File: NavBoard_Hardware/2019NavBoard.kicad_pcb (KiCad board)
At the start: 2 copper layers, 61 x 88.7 mm, 21 parts, among them J1 Conn_Coaxial, U2 12mm_Coin_Battery_Cell_Holder, U5 FGPMMOPA6H

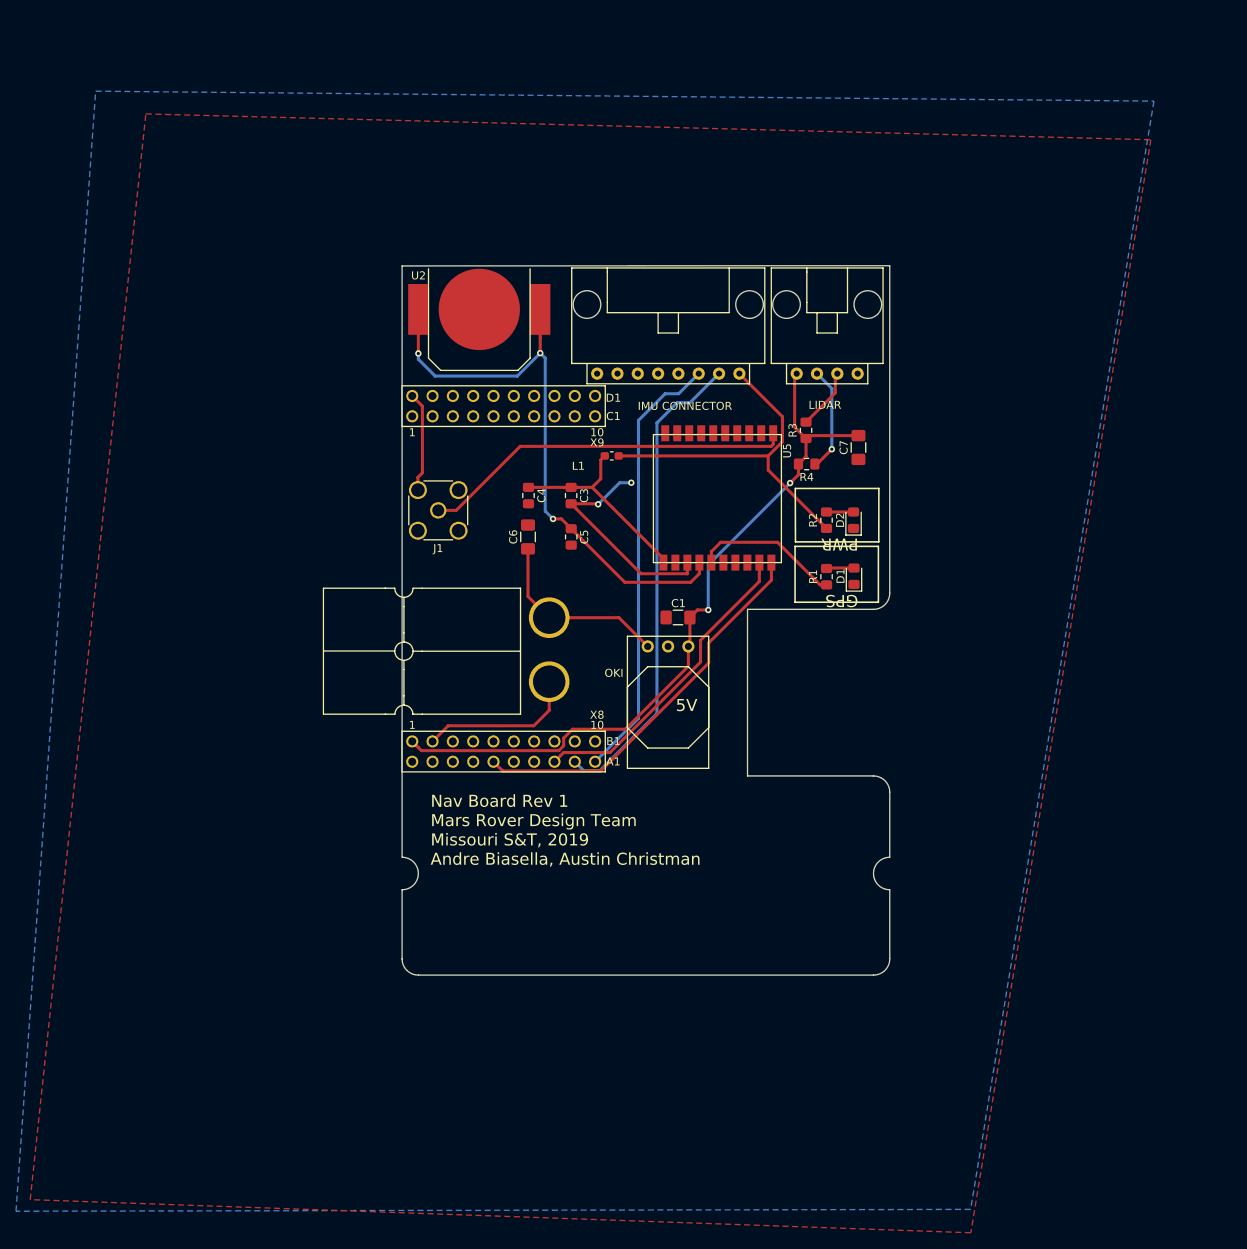
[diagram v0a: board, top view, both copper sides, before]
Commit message: Editied schematic and made PCB
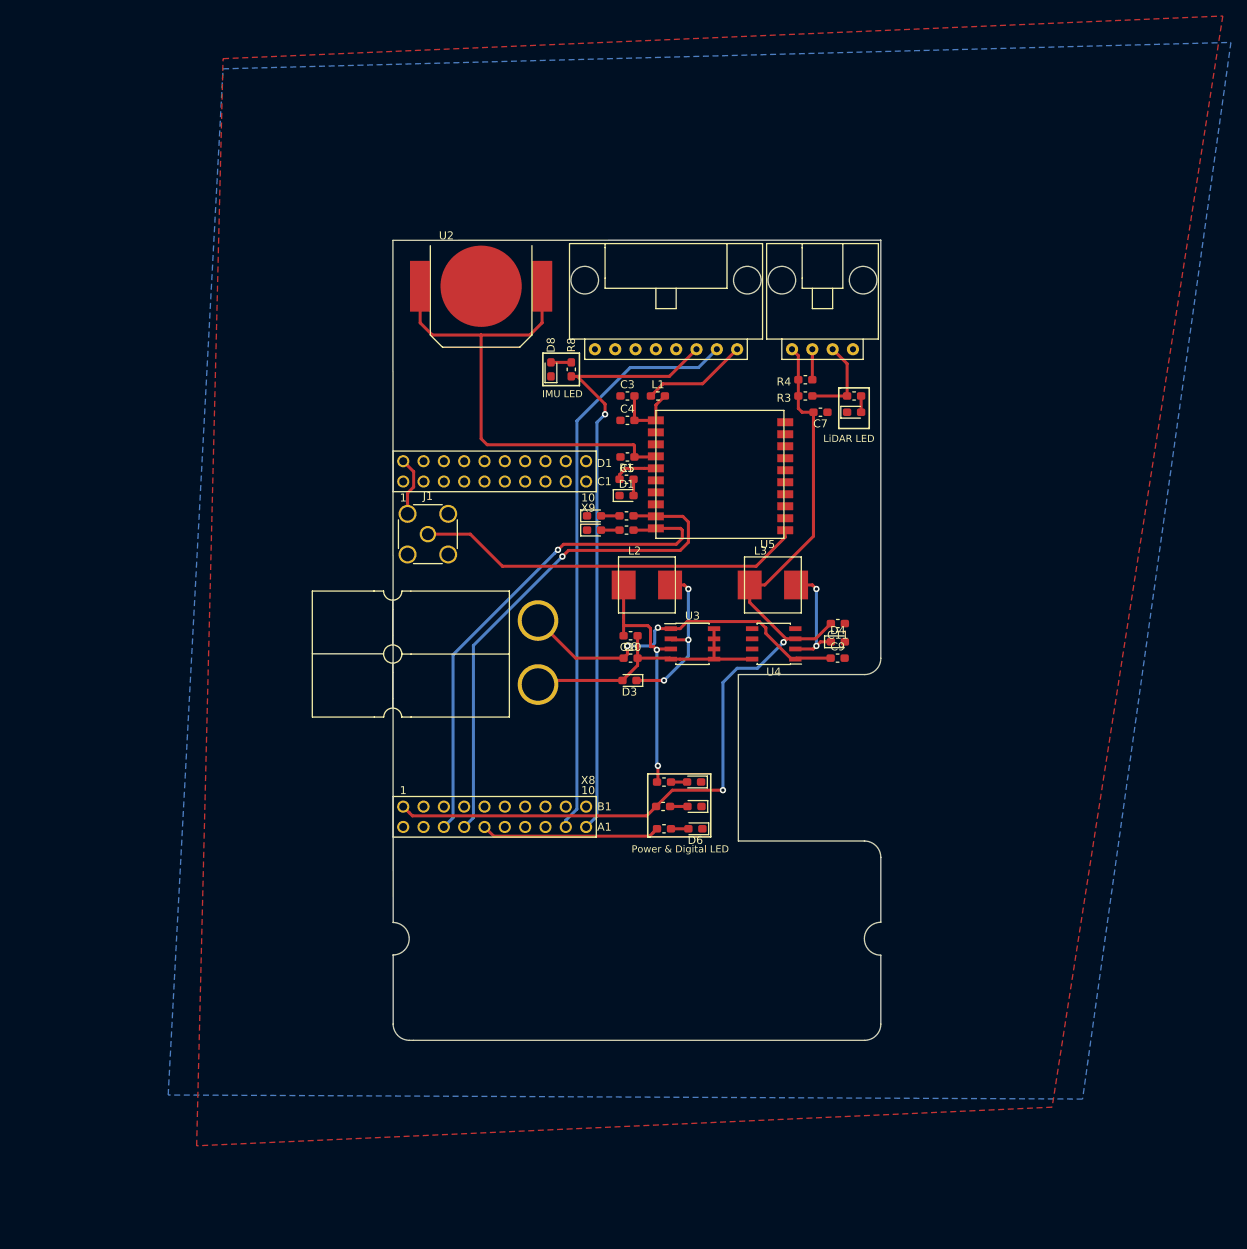
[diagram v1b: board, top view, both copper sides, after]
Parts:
- removed C1, C6: 10uF, Capacitor_SMD:C_1206_3216Metric_Pad1.42x1.75mm_HandSolder
- removed C2: OKI, MRDT_Devices:OKI_Horizontal
- removed IMU CONNECTOR: Molex_SL_08, MRDT_Connectors:MOLEX_SL_08_Horizontal
- removed LIDAR: LiDAR, MRDT_Connectors:MOLEX_SL_04_Horizontal
- added C10: 10u, Capacitor_SMD:C_0603_1608Metric_Pad1.05x0.95mm_HandSolder, F.Cu at (144.9, 101.9)
- added C11: 10u, Capacitor_SMD:C_0603_1608Metric_Pad1.05x0.95mm_HandSolder, F.Cu at (170.8, 100.3)
- added C8: 10u, Capacitor_SMD:C_0603_1608Metric_Pad1.05x0.95mm_HandSolder, F.Cu at (144.9, 104.6)
- added C9: 10u, Capacitor_SMD:C_0603_1608Metric_Pad1.05x0.95mm_HandSolder, F.Cu at (170.8, 104.6)
- added Conn2: LiDAR, MRDT_Connectors:MOLEX_SL_04_Horizontal, F.Cu at (168.9, 66.0)
- added Conn3: Molex_SL_08, MRDT_Connectors:MOLEX_SL_08_Horizontal, F.Cu at (149.4, 66.0)
- added D10: PWR, LED_SMD:LED_0603_1608Metric_Pad1.05x0.95mm_HandSolder, F.Cu at (140.3, 86.9)
- added D3: D_Schottky, Diode_SMD:D_0603_1608Metric_Pad1.05x0.95mm_HandSolder, F.Cu at (144.8, 107.4)
- added D4: D_Schottky, Diode_SMD:D_0603_1608Metric_Pad1.05x0.95mm_HandSolder, F.Cu at (170.8, 102.6)
- added D5: PWR, LED_SMD:LED_0603_1608Metric_Pad1.05x0.95mm_HandSolder, F.Cu at (152.9, 123.2)
- added D6: PWR, LED_SMD:LED_0603_1608Metric_Pad1.05x0.95mm_HandSolder, F.Cu at (153.0, 126.0)
- added D7: PWR, LED_SMD:LED_0603_1608Metric_Pad1.05x0.95mm_HandSolder, F.Cu at (172.9, 73.9)
- added D8: PWR, LED_SMD:LED_0603_1608Metric_Pad1.05x0.95mm_HandSolder, F.Cu at (135.0, 68.6)
- added D9: PWR, LED_SMD:LED_0603_1608Metric_Pad1.05x0.95mm_HandSolder, F.Cu at (140.3, 88.6)
- added L2: 47u, MRDT_Passives:ETQ-P4M470YFN_Inductor, F.Cu at (147.0, 95.5)
- added L3: 47u, MRDT_Passives:ETQ-P4M470YFN_Inductor, F.Cu at (162.7, 95.5)
- added R10: 500, Resistor_SMD:R_0603_1608Metric_Pad1.05x0.95mm_HandSolder, F.Cu at (144.4, 86.9)
- added R5: 500, Resistor_SMD:R_0603_1608Metric_Pad1.05x0.95mm_HandSolder, F.Cu at (149.0, 123.2)
- added R6: 500, Resistor_SMD:R_0603_1608Metric_Pad1.05x0.95mm_HandSolder, F.Cu at (149.1, 126.0)
- added R7: 500, Resistor_SMD:R_0603_1608Metric_Pad1.05x0.95mm_HandSolder, F.Cu at (172.9, 71.9)
- added R8: 500, Resistor_SMD:R_0603_1608Metric_Pad1.05x0.95mm_HandSolder, F.Cu at (137.5, 68.6)
- added R9: 500, Resistor_SMD:R_0603_1608Metric_Pad1.05x0.95mm_HandSolder, F.Cu at (144.4, 88.6)
- added U3: AP1059, Package_SO:SOIC-8_3.9x4.9mm_P1.27mm, F.Cu at (152.7, 102.9)
- added U4: AP1059, Package_SO:SOIC-8_3.9x4.9mm_P1.27mm, F.Cu at (162.8, 102.9)
- C3, C4, C5: footprint Capacitor_SMD:C_0805_2012Metric_Pad1.15x1.40mm_HandSolder -> Capacitor_SMD:C_0603_1608Metric_Pad1.05x0.95mm_HandSolder
- C7: footprint Capacitor_SMD:C_1206_3216Metric_Pad1.42x1.75mm_HandSolder -> Capacitor_SMD:C_0603_1608Metric_Pad1.05x0.95mm_HandSolder
- D1, D2: footprint LED_SMD:LED_0805_2012Metric_Pad1.15x1.40mm_HandSolder -> LED_SMD:LED_0603_1608Metric_Pad1.05x0.95mm_HandSolder
- R1, R3, R4: footprint Resistor_SMD:R_0805_2012Metric_Pad1.15x1.40mm_HandSolder -> Resistor_SMD:R_0603_1608Metric_Pad1.05x0.95mm_HandSolder
- R2: value 1K -> 500; footprint Resistor_SMD:R_0805_2012Metric_Pad1.15x1.40mm_HandSolder -> Resistor_SMD:R_0603_1608Metric_Pad1.05x0.95mm_HandSolder
- moved R2 38.5 mm to (149.1, 120.1), turned to 0 degrees
- moved D2 38.3 mm to (152.9, 120.1), turned to 180 degrees
- moved D1 30.2 mm to (144.4, 84.3), turned to 0 degrees
- moved R1 27.8 mm to (144.4, 82.3), turned to 0 degrees
- moved U5 17.8 mm to (148.1, 74.9), turned to 0 degrees
- moved C4 15.5 mm to (144.5, 74.9), turned to 0 degrees
- moved C3 14.3 mm to (144.5, 71.9), turned to 0 degrees
- moved C5 12.2 mm to (144.5, 79.5), turned to 180 degrees
- moved R4 10.5 mm to (166.8, 69.8)
- moved L1 9.45 mm to (148.3, 71.9), turned to 0 degrees
- moved U1 8.23 mm to (115.2, 127.0)
- moved C7 6.48 mm to (168.7, 73.9), turned to 180 degrees
- moved R3 4.29 mm to (166.8, 71.9), turned to 0 degrees
- moved J1 3.24 mm to (119.6, 89.2), turned to 0 degrees
- moved U2 2.90 mm to (126.2, 58.2)
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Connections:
- net 1PPS renamed Net-(U5-Pad13)
- net Net-(J1-Pad1) renamed /EXAnt
- C3 pad 1: Net-(C3-Pad1) -> GND
- C3 pad 2: GND -> Net-(C3-Pad2)
- C4 pad 1: Net-(C3-Pad1) -> GND
- C4 pad 2: GND -> Net-(C3-Pad2)
- Conn1 pad 1: GND -> Net-(C10-Pad1)
- L1 pad 2: Net-(C3-Pad1) -> Net-(C3-Pad2)
- U1 pad PC4: Net-(U1-PadPC4) -> TivaRX(7)
- U1 pad PC5: Net-(U1-PadPC5) -> TivaTX(7)
- U1 pad PC6: RX(7) -> Error_LED
- U1 pad PC7: TX(7) -> Net-(U1-PadPC7)
- U5 pad 1: Net-(C3-Pad1) -> Net-(C3-Pad2)
- U5 pad 10: RX(7) -> TivaRX(7)
- U5 pad 9: TX(7) -> TivaTX(7)
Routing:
- net TivaTX(7): track 0.00 -> 65.1 mm, vias 0 -> 1
- net TivaRX(7): track 0.00 -> 64.0 mm, vias 0 -> 1
- net GND: track 62.2 -> 7.44 mm, vias 2 -> 0
- net RX(7): track 48.8 -> 0.00 mm
- net TX(7): track 38.9 -> 0.00 mm
- net Net-(C10-Pad1): track 0.00 -> 35.3 mm
- net +5V: track 90.3 -> 116.3 mm
- net Net-(C3-Pad1): track 25.7 -> 0.00 mm
- net Error_LED: track 0.00 -> 22.4 mm
- net SDA(0): track 54.9 -> 75.8 mm, vias 0 -> 1
- net Net-(C8-Pad1): track 23.5 -> 44.4 mm, vias 0 -> 2
- net Net-(D3-Pad1): track 0.00 -> 20.9 mm, vias 0 -> 3
- net Net-(D4-Pad1): track 0.00 -> 14.7 mm, vias 0 -> 2
- net Net-(R1-Pad1): track 18.5 -> 5.45 mm
- net VBACKUP: track 74.2 -> 62.2 mm, vias 3 -> 0
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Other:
- board size 61 x 88.7 mm -> 61 x 100 mm
- board text added: "IMU LED"
- board text added: "LiDAR LED"
- board text added: "Power & Digital LED"
- board text removed: "5V"
- board text removed: "GPS"
- board text removed: "Nav Board Rev 1 Mars Rover Design Team Missouri S&T, 2019 Andre Biasella, Austin Christman"
- board text removed: "PWR"

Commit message: edit PCB
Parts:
- added G***: LOGO, MRDT_Silkscreens:MRDT_Logo_10mm, F.Cu at (120.9, 72.4)

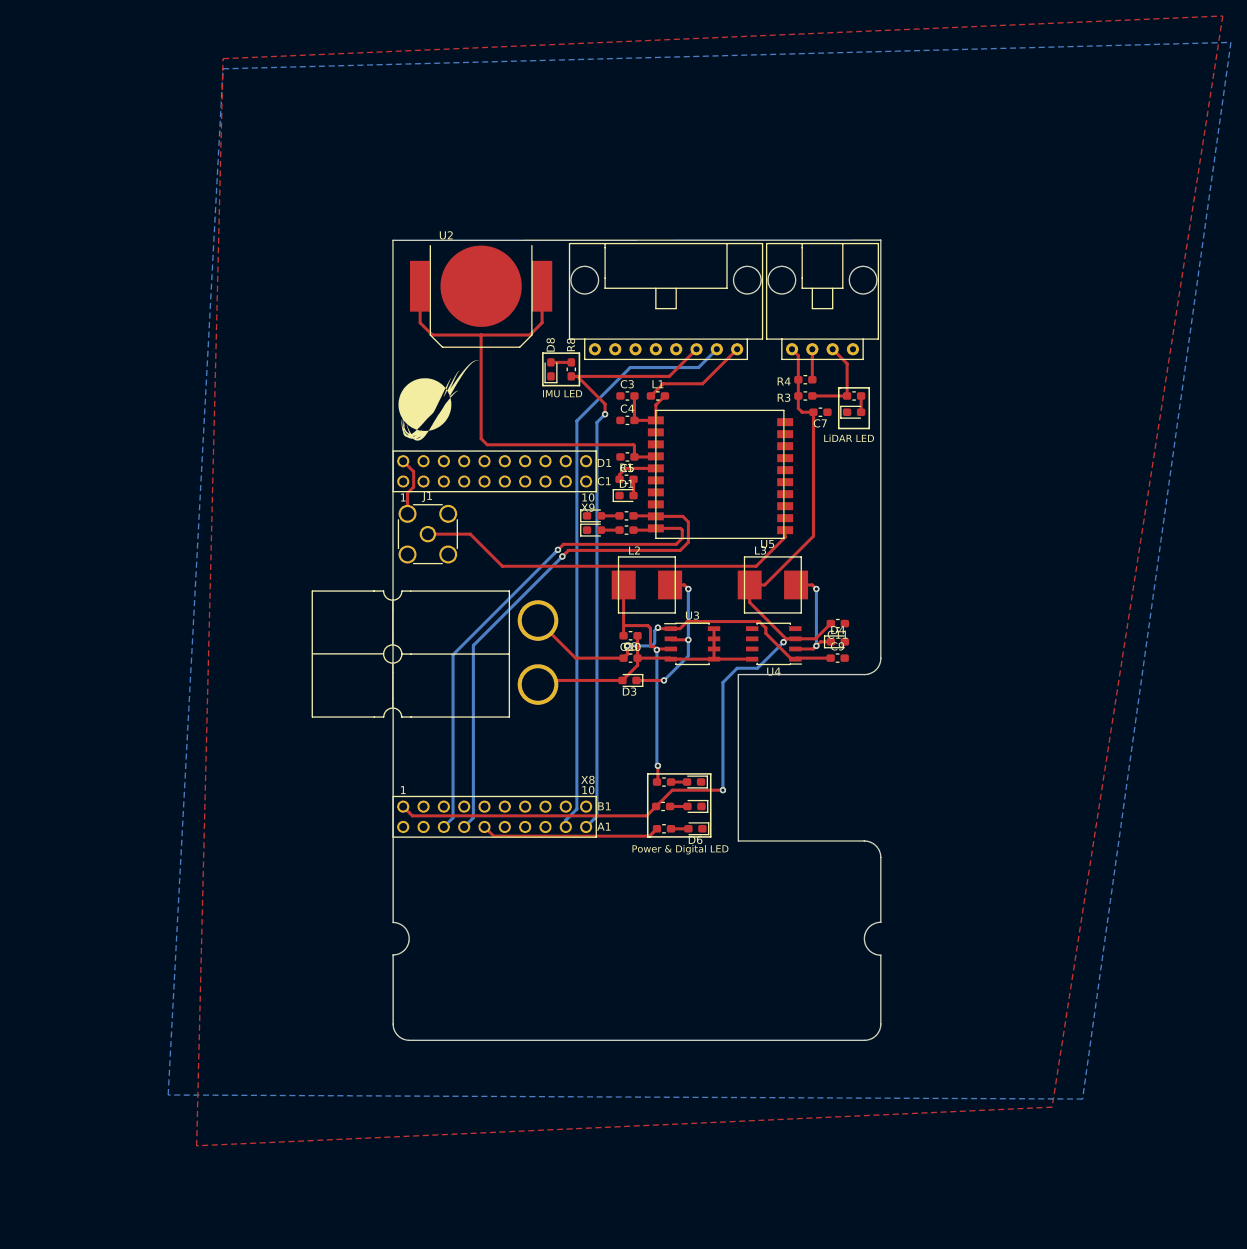
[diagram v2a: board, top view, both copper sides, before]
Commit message: Fixed traces
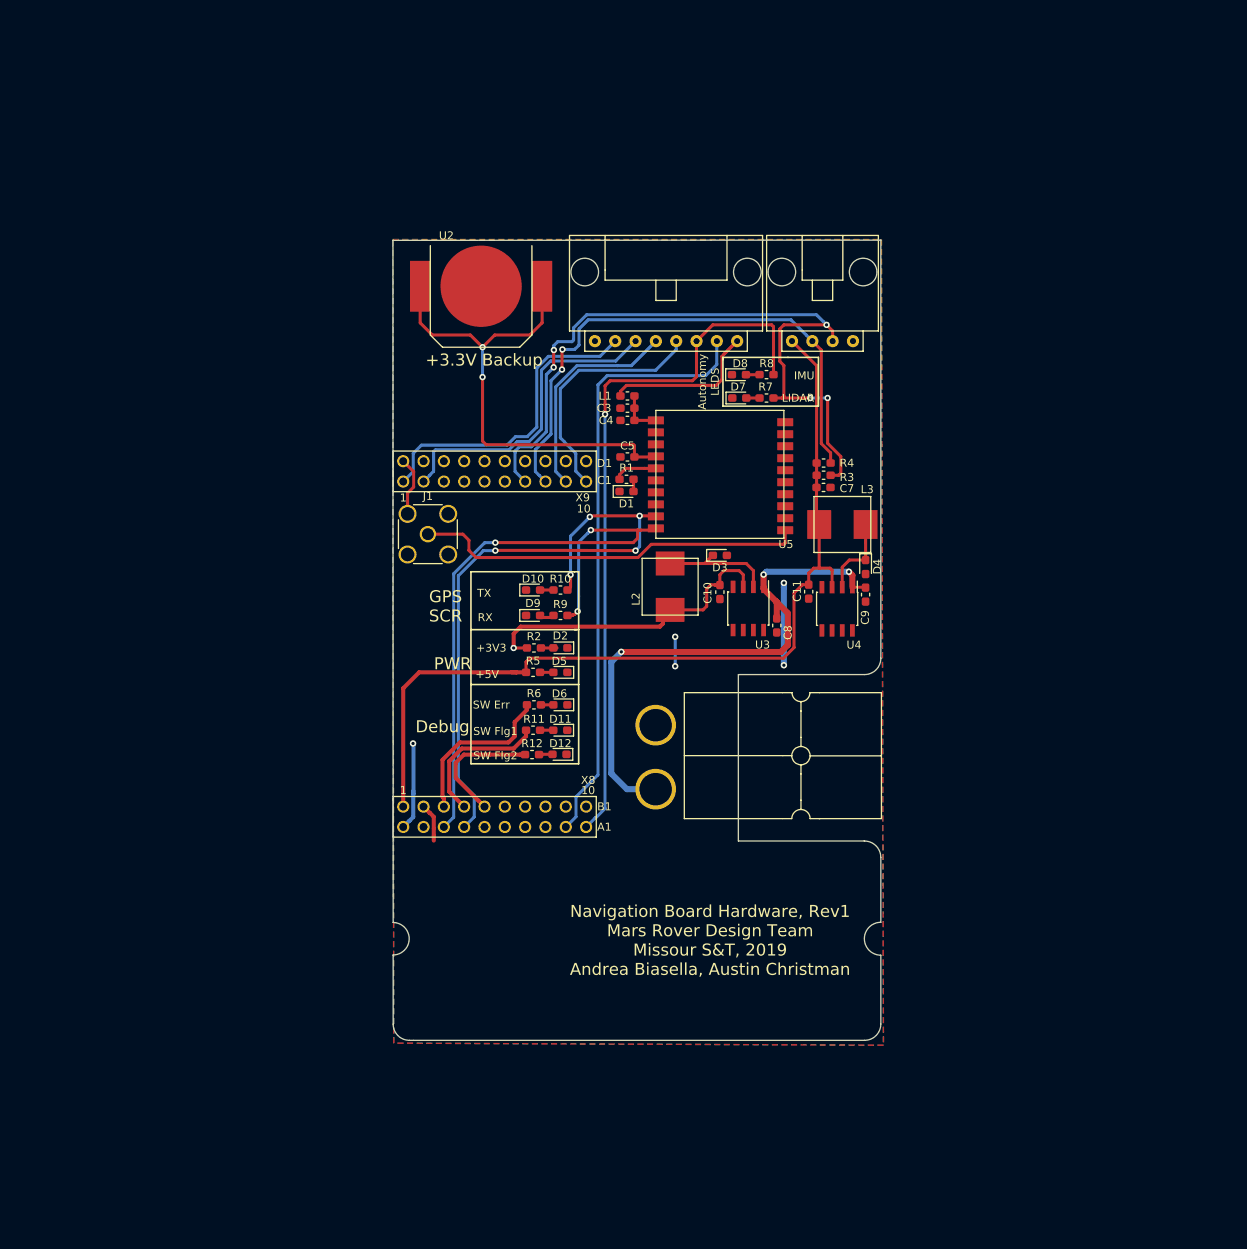
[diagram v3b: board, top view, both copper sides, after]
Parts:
- removed G***: LOGO, MRDT_Silkscreens:MRDT_Logo_10mm
- added D11: PWR, LED_SMD:LED_0603_1608Metric_Pad1.05x0.95mm_HandSolder, F.Cu at (136.1, 113.7)
- added D12: PWR, LED_SMD:LED_0603_1608Metric_Pad1.05x0.95mm_HandSolder, F.Cu at (136.0, 116.7)
- added R11: 500, Resistor_SMD:R_0603_1608Metric_Pad1.05x0.95mm_HandSolder, F.Cu at (132.7, 113.7)
- added R12: 500, Resistor_SMD:R_0603_1608Metric_Pad1.05x0.95mm_HandSolder, F.Cu at (132.6, 116.7)
- moved R8 24.4 mm to (161.9, 69.2), turned to 180 degrees
- moved D5 23.7 mm to (136.1, 106.4)
- moved D2 23.7 mm to (136.1, 103.4)
- moved D8 23.5 mm to (158.5, 69.2), turned to 0 degrees
- moved R2 23.4 mm to (132.8, 103.4)
- moved R5 23.4 mm to (132.7, 106.4)
- moved D6 22.9 mm to (136.1, 110.5)
- moved R6 22.5 mm to (132.8, 110.5)
- moved Conn1 22.1 mm to (151.6, 109.0), turned to 180 degrees
- moved D3 19.3 mm to (156.1, 91.8), turned to 0 degrees
- moved C8 18.7 mm to (163.2, 100.6), turned to 270 degrees
- moved D7 14.5 mm to (158.5, 72.1)
- moved R9 13.5 mm to (136.2, 99.3)
- moved D9 13.1 mm to (132.7, 99.3)
- moved C10 12.4 mm to (156.1, 96.4), turned to 90 degrees
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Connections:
- C10 pad 1: Net-(C10-Pad1) -> GND
- C8 pad 2: Net-(C10-Pad1) -> GND
- Conn1 pad 1: Net-(C10-Pad1) -> GND
- D3 pad 2: Net-(C10-Pad1) -> GND
- U1 pad PC6: Error_LED -> Net-(U1-PadPC6)
- U1 pad PE0: Net-(U1-PadPE0) -> Error_LED
- U1 pad PE1: Net-(U1-PadPE1) -> SW_Flg1
- U1 pad PE2: Net-(U1-PadPE2) -> SW_Flg2
- U1 pad PF1: (no net) -> INT2AG
- U1 pad PF2: (no net) -> INT1AG
- U1 pad PF3: (no net) -> Net-(U1-PadPF3)
- U1 pad PG0: (no net) -> Net-(U1-PadPG0)
- U1 pad PL0: (no net) -> LIDAR_SDA
- U1 pad PL1: (no net) -> LIDAR_SCL
- U1 pad PL2: (no net) -> INTM
- U1 pad PL3: (no net) -> DRDYM
- U1 pad PL4: (no net) -> Net-(U1-PadPL4)
- U1 pad PL5: (no net) -> Net-(U1-PadPL5)
- U3 pad 4: Net-(C10-Pad1) -> GND
- U3 pad 5: Net-(C10-Pad1) -> GND
- U3 pad 6: Net-(C10-Pad1) -> GND
- U3 pad 7: Net-(C10-Pad1) -> GND
- U3 pad 8: Net-(C10-Pad1) -> GND
- U4 pad 8: Net-(C10-Pad1) -> GND
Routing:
- net LIDAR_SDA: track 10.9 -> 93.1 mm, vias 0 -> 5
- net LIDAR_SCL: track 3.81 -> 69.7 mm, vias 0 -> 2
- net INT1AG: track 0.00 -> 39.5 mm
- net INT2AG: track 0.00 -> 39.4 mm
- net Net-(C10-Pad1): track 35.3 -> 0.00 mm
- net DRDYM: track 0.00 -> 30.5 mm
- net +3V3: track 45.2 -> 72.7 mm
- net INTM: track 0.00 -> 27.2 mm
- net Net-(C8-Pad1): track 44.4 -> 70.1 mm, vias 2 -> 3
- net GND: track 7.44 -> 26.2 mm, vias 0 -> 4
- net SW_Flg1: track 0.00 -> 18.1 mm
- net SW_Flg2: track 0.00 -> 16.1 mm
- net TivaRX(7): track 64.0 -> 78.5 mm, vias 1 -> 3
- net TivaTX(7): track 65.1 -> 79.4 mm, vias 1 -> 5
- net SDA(0): track 75.8 -> 89.1 mm
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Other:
- board text added: "+3.3V Backup"
- board text added: "+3V3"
- board text added: "+5V"
- board text added: "4 3 2 1"
- board text added: "8 7 6 5 4 3 2 1"
- board text added: "Autonomy LEDS"
- board text added: "DRDYM"
- board text added: "Debug"
- board text added: "GND"
- board text added: "GPS SCR"
- board text added: "IMU"
- board text added: "INT1AG"
- board text added: "INT2AG"
- board text added: "INTM"
- board text added: "LIDAR"
- board text added: "Navigation Board Hardware, Rev1 Mars Rover Design Team Missour S&T, 2019 Andrea Biasella, Austin Christman"
- board text added: "PWR"
- board text added: "RX"
- board text added: "SCL"
- board text added: "SDA"
- board text added: "SW Err"
- board text added: "SW Flg1"
- board text added: "SW Flg2"
- board text added: "TX"
- board text removed: "IMU LED"
- board text removed: "LiDAR LED"
- board text removed: "Power & Digital LED"
